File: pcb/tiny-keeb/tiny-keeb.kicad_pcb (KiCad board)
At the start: 2 copper layers, 146 x 61.6 mm, 123 parts, among them J2 Conn_01x20_Socket, SW1 SW_RCTRL, SW10 SW_A, SW11 SW_X, SW12 SW_LWIN, SW13 SW_2, SW14 SW_E, SW15 SW_S, SW16 SW_C, SW17 SW_LALT, SW18 SW_', SW19 SW_3, SW2 SW_ESC, SW20 SW_R, SW21 SW_D, SW22 SW_V, SW23 SW_Z, SW24 SW_/, SW25 SW_4, SW26 SW_T, SW27 SW_F, SW28 SW_B, SW29 SW_-, SW3 SW_TAB, SW31 SW_5, SW32 SW_Y, SW33 SW_G, SW34 SW_N, SW35 SW_], SW37 SW_6, SW38 SW_U, SW39 SW_H, SW4 SW_CAPS, SW40 SW_M, SW41 SW_SPACE, SW43 SW_7, SW44 SW_I, SW45 SW_J, SW46 SW_,, SW49 SW_8, SW5 SW_LSHIFT, SW50 SW_O, SW51 SW_K, SW52 SW_., SW55 SW_9, SW56 SW_P, SW57 SW_L, SW58 SW_RSHIFT, SW59 SW_RALT, SW6 SW_LCTRL, SW61 SW_0, SW62 SW_[, SW63 SW_;, SW65 SW_RWIN, SW66 SW_FN, SW67 SW_=, SW7 SW_Q, SW72 SW_BACKSPACE, SW73 SW_\, SW74 SW_ENTER, SW8 SW_1, SW9 SW_W

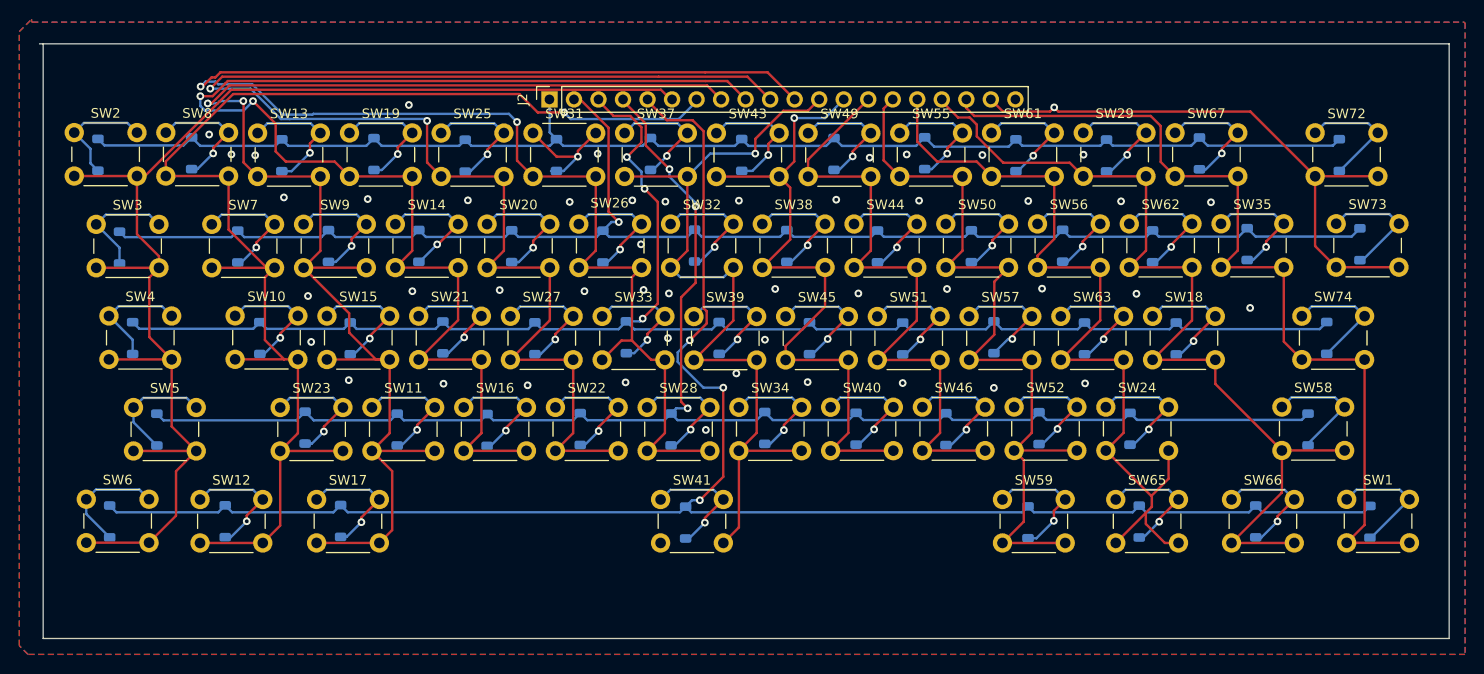
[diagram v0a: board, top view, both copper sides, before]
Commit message: pcb close to done, housing in progress, caps not started
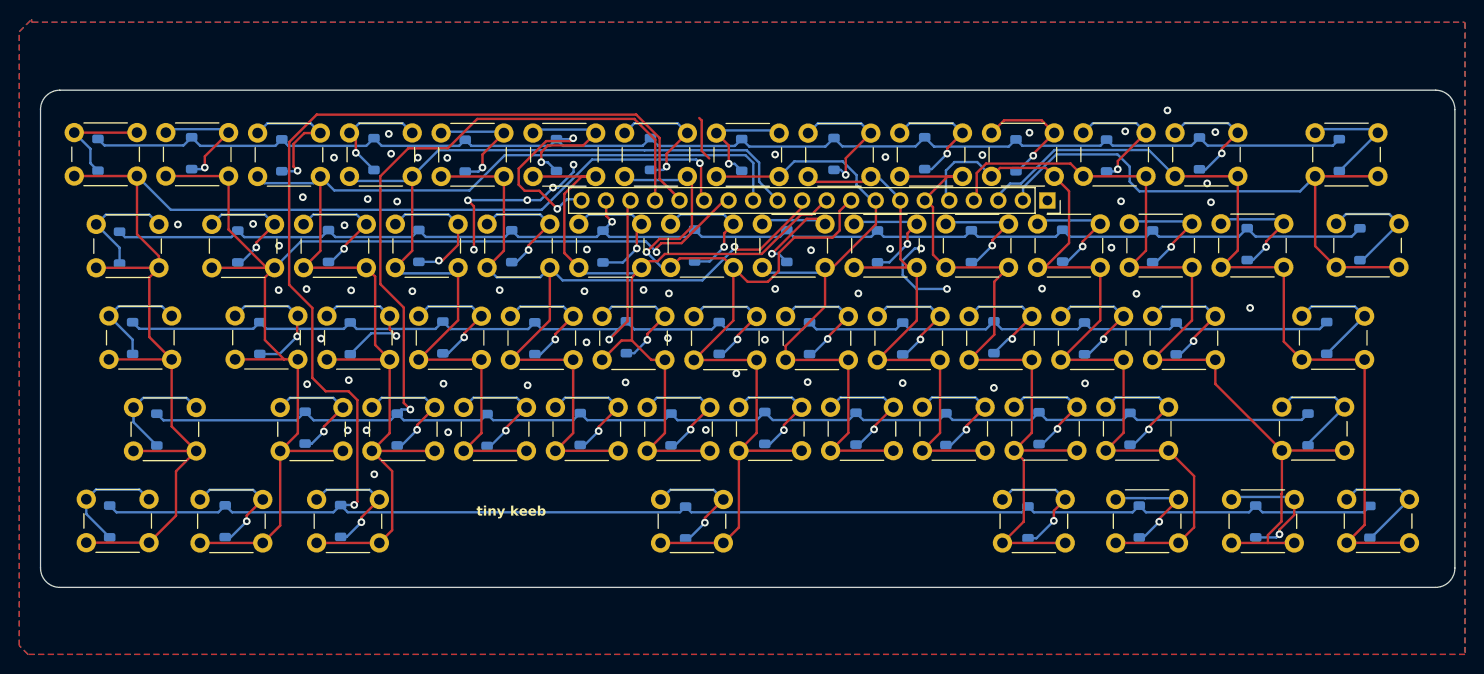
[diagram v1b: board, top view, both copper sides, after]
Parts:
- added G***: LOGO, LOGO, B.Cu at (69.1, 92.3)
- moved J2 52.6 mm to (124.2, 59.4), turned to -90 degrees
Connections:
- J2 pad 1: /row0 -> GND
- J2 pad 10: /col4 -> /col5
- J2 pad 11: /col5 -> /col4
- J2 pad 12: /col6 -> /col3
- J2 pad 13: /col7 -> /col2
- J2 pad 14: /col8 -> /col1
- J2 pad 15: /col9 -> /col0
- J2 pad 16: /col10 -> /row4
- J2 pad 17: /col11 -> /row3
- J2 pad 18: /col12 -> /row2
- J2 pad 19: /col13 -> /row1
- J2 pad 2: /row1 -> /col13
- J2 pad 20: GND -> /row0
- J2 pad 3: /row2 -> /col12
- J2 pad 4: /row3 -> /col11
- J2 pad 5: /row4 -> /col10
- J2 pad 6: /col0 -> /col9
- J2 pad 7: /col1 -> /col8
- J2 pad 8: /col2 -> /col7
- J2 pad 9: /col3 -> /col6
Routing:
- net /col5: track 160.4 -> 80.7 mm, vias 2 -> 0
- net /col4: track 147.3 -> 89.4 mm, vias 2 -> 1
- net /row4: track 187.1 -> 225.7 mm, vias 3 -> 1
- net /col3: track 137.5 -> 100.7 mm, vias 2 -> 0
- net GND: track 0.00 -> 32.0 mm, vias 47 -> 65
- net /row3: track 163.8 -> 190.9 mm, vias 3 -> 1
- net /col2: track 144.6 -> 126.7 mm, vias 2 -> 0
- net /row0: track 140.9 -> 155.2 mm, vias 0 -> 2
- net /row1: track 153.0 -> 140.0 mm
- net /row2: track 160.7 -> 147.9 mm, vias 3 -> 1
- net /col6: track 86.5 -> 99.2 mm
- net /col1: track 136.9 -> 126.8 mm
- net /col0: track 135.5 -> 142.7 mm, vias 0 -> 1
- net /col8: track 68.1 -> 61.0 mm
- net /col9: track 84.0 -> 77.6 mm
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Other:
- board size 146 x 61.6 mm -> 146.5 x 51.5 mm
- board text added: "C00"
- board text added: "C01"
- board text added: "C02"
- board text added: "C03"
- board text added: "C04"
- board text added: "C05"
- board text added: "C06"
- board text added: "C07"
- board text added: "C08"
- board text added: "C09"
- board text added: "C10"
- board text added: "C11"
- board text added: "C12"
- board text added: "C13"
- board text added: "GND"
- board text added: "R00"
- board text added: "R01"
- board text added: "R02"
- board text added: "R03"
- board text added: "R04"
- board text added: "tiny keeb"
- board text added: "tiny keeb - V1.0 Brian Hill 2024 github.com/TrojanPinata/tiny-keeb"
- board text added: "to pico"

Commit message: finished housing, keycaps, and pcb - waiting to order switches and pcb
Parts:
- added SW30: SW_SPACE2, Button_Switch_THT:SW_PUSH_6mm_square_top, F.Cu at (73.6, 94.9)
- SW1, SW10, SW11, SW12, SW13, SW14, SW15, SW16, SW17, SW18, SW19, SW2, SW20, SW21, SW22, SW23, SW24, SW25, SW26, SW27, SW28, SW29, SW3, SW31, SW32, SW33, SW34, SW35, SW37, SW38, SW39, SW4, SW40, SW41, SW43, SW44, SW45, SW46, SW49, SW5, SW50, SW51, SW52, SW55, SW56, SW57, SW58, SW59, SW6, SW61, SW62, SW63, SW65, SW66, SW67, SW7, SW72, SW73, SW74, SW8, SW9: footprint Button_Switch_THT:SW_PUSH_6mm -> Button_Switch_THT:SW_PUSH_6mm_square_top
- moved G*** 43.5 mm to (112.5, 93.0)
- moved D41 22.5 mm to (64.2, 94.2)
- moved SW41 15.6 mm to (99.7, 90.4)
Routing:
- net Net-(D41-A): track 13.2 -> 48.3 mm
- net /col6: track 99.2 -> 131.8 mm
- net Net-(D59-A): track 13.4 -> 12.8 mm
